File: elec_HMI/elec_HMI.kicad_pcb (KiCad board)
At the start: 2 copper layers, 20 x 20 mm, 17 parts, among them J1 JST SH, J7 JST SH, U1 AS5600L

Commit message: [update] Angle+IMU are routed ERC OK
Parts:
- removed C25: 100n, Capacitor_SMD:C_0402_1005Metric
- removed D1: SP0503BAHT, Package_TO_SOT_SMD:SOT-143
- removed FID1, FID2, FID3: DNP Fiducial, Fiducial:Fiducial_1mm_Mask2mm
- removed G1: qwiic_Logo, Library_Pollen:Logo_qwiic_5mm
- removed H2: Logo HF 2025, Library_Pollen:Logo_HF_2025
- removed H3: DNP Logo Pollen 2021, Library_Pollen:Logo_Pollen_2021_sq
- removed H4: Mounting Holes M2,5, MountingHole:MountingHole_2.7mm_M2.5_ISO7380_Pad_TopBottom
- removed H5: MountingHole_Pad, MountingHole:MountingHole_2.7mm_M2.5_ISO7380_Pad_TopBottom
- removed H6, H7: Centering Hole 2 mm, Library_Pollen:MountingHole_2.0mm
- removed J1, J7: JST SH, Connector_JST:JST_SH_SM04B-SRSS-TB_1x04-1MP_P1.00mm_Horizontal
- removed R1, R2: DNP-10k, Resistor_SMD:R_0402_1005Metric
- removed U1: AS5600L, Package_SO:SOIC-8_3.9x4.9mm_P1.27mm
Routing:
- net +3V3: track 35.5 -> 0.00 mm, vias 2 -> 0
- net Net-(J1-Pin_3): track 22.2 -> 0.00 mm, vias 1 -> 0
- net Net-(J1-Pin_4): track 20.3 -> 0.00 mm, vias 1 -> 0
- net GND: track 9.87 -> 0.00 mm, vias 23 -> 0
- removed copper zone on B.Cu, net GND
- removed copper zone on F.Cu, net GND
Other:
- board outline removed
- board text removed: "!! Prévoir une place pour marquer l'adresse I2C du capteur d'angle"
- board text removed: "ASE001189-A1 angle_sensor"

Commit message: [added] Wiring Diagrams
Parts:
- added C1: 100n 6V3, Capacitor_SMD:C_0402_1005Metric, F.Cu at (127.4, 72.7)
- added D1: SP0503BAHT, Package_TO_SOT_SMD:SOT-143, F.Cu at (142.0, 63.8)
- added D2: Green, LED_SMD:LED_0603_1608Metric, F.Cu at (133.2, 50.4)
- added D3: Red, LED_SMD:LED_0603_1608Metric, F.Cu at (133.2, 53.0)
- added D4: Blue, LED_SMD:LED_0603_1608Metric, F.Cu at (133.2, 55.6)
- added FID1: DNP Fiducial, Fiducial:Fiducial_1mm_Mask2mm, F.Cu at (162.4, 73.3)
- added FID2: DNP Fiducial, Fiducial:Fiducial_1mm_Mask2mm, F.Cu at (133.7, 46.2)
- added FID3: DNP Fiducial, Fiducial:Fiducial_1mm_Mask2mm, F.Cu at (156.4, 46.0)
- added G1: qwiic_Logo, Library_Pollen:Logo_qwiic_5mm, F.Cu at (127.8, 58.7)
- added H2: Logo HF 2025, Library_Pollen:Logo_HF_2025, F.Cu at (161.4, 77.8)
- added H3: DNP Logo Pollen 2021, Library_Pollen:Logo_Pollen_2021_sq, F.Cu at (155.3, 54.6)
- added H4: Mounting Holes M2,5, MountingHole:MountingHole_2.7mm_M2.5_ISO7380_Pad_TopBottom, F.Cu at (127.4, 80.9)
- added H5: MountingHole_Pad, MountingHole:MountingHole_2.7mm_M2.5_ISO7380_Pad_TopBottom, F.Cu at (161.4, 46.5)
- added H6: Centering Hole 2 mm, Library_Pollen:MountingHole_2.0mm, F.Cu at (127.4, 46.6)
- added H7: Centering Hole 2 mm, Library_Pollen:MountingHole_2.0mm, F.Cu at (161.4, 80.6)
- added J1: JST SH, Connector_JST:JST_SH_SM04B-SRSS-TB_1x04-1MP_P1.00mm_Horizontal, F.Cu at (160.8, 63.7)
- added J2: JST SH, Connector_JST:JST_SH_SM04B-SRSS-TB_1x04-1MP_P1.00mm_Horizontal, F.Cu at (128.4, 64.1)
- added R1: 0R, Resistor_SMD:R_0402_1005Metric, F.Cu at (127.5, 74.4)
- added R10: 470R, Resistor_SMD:R_0402_1005Metric, F.Cu at (133.2, 61.2)
- added R2: 0R, Resistor_SMD:R_0402_1005Metric, F.Cu at (127.5, 76.3)
- added R3: DNP-10k, Resistor_SMD:R_0402_1005Metric, F.Cu at (134.2, 64.3)
- added R4: DNP-10k, Resistor_SMD:R_0402_1005Metric, F.Cu at (134.2, 66.3)
- added R5: 0R, Resistor_SMD:R_0402_1005Metric, F.Cu at (127.5, 77.6)
- added R6: 10k, Resistor_SMD:R_0402_1005Metric, F.Cu at (147.6, 63.2)
- added R7: 10k, Resistor_SMD:R_0402_1005Metric, F.Cu at (147.6, 65.1)
- added R8: 470R, Resistor_SMD:R_0402_1005Metric, F.Cu at (133.2, 57.3)
- added R9: 470R, Resistor_SMD:R_0402_1005Metric, F.Cu at (133.2, 59.2)
- added SW1: SW_SPST, Button_Switch_Keyboard:SW_Cherry_MX_1.00u_PCB, F.Cu at (147.6, 49.1)
- added SW2: SW_SPST, Button_Switch_Keyboard:SW_Cherry_MX_1.00u_PCB, F.Cu at (147.5, 68.7)
- added TP1: TestPoint, TestPoint:TestPoint_Loop_D2.50mm_Drill1.0mm_LowProfile, F.Cu at (161.7, 70.1)
- added TP2: TestPoint, TestPoint:TestPoint_Loop_D2.50mm_Drill1.0mm_LowProfile, F.Cu at (158.3, 72.3)
- added U1: PCF8574ATS, Package_SO:SSOP-20_4.4x6.5mm_P0.65mm, F.Cu at (132.7, 73.1)
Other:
- board outline added: 40 x 40 mm

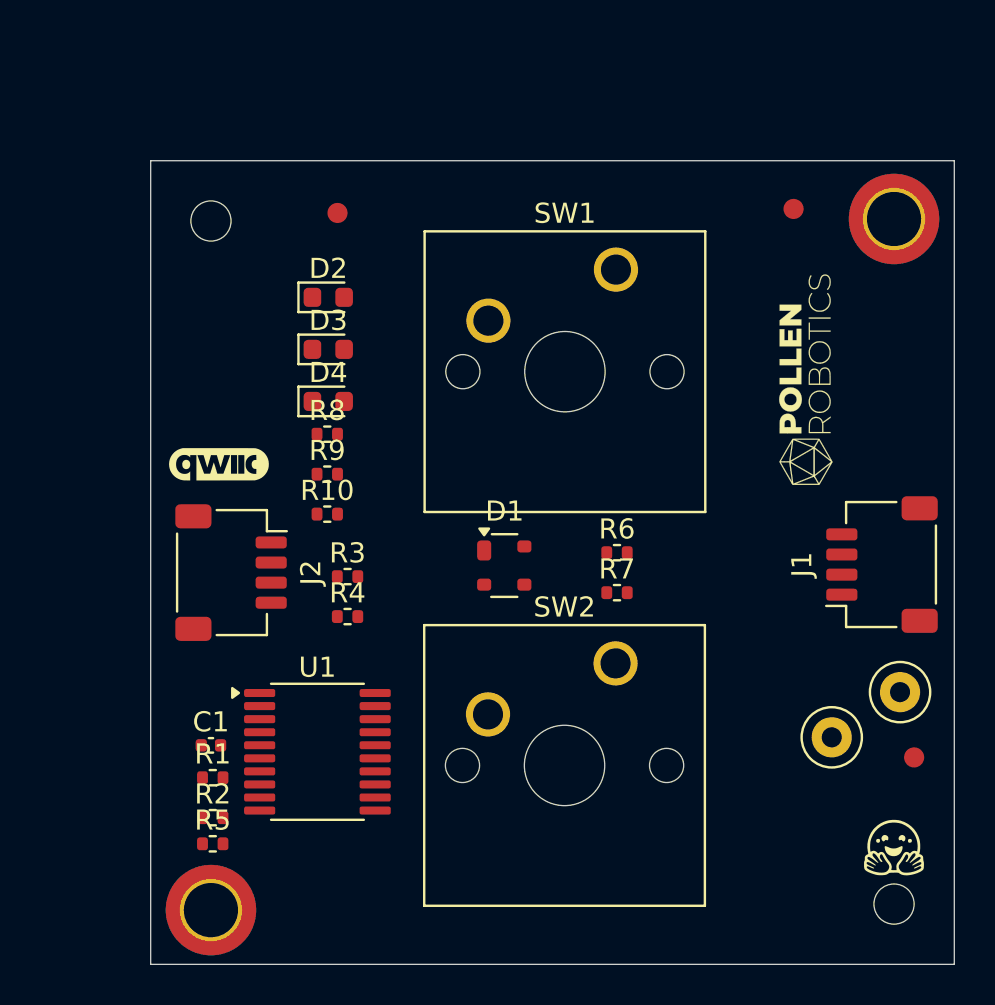
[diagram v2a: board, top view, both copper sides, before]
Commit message: [update] Mechanical adaptations.
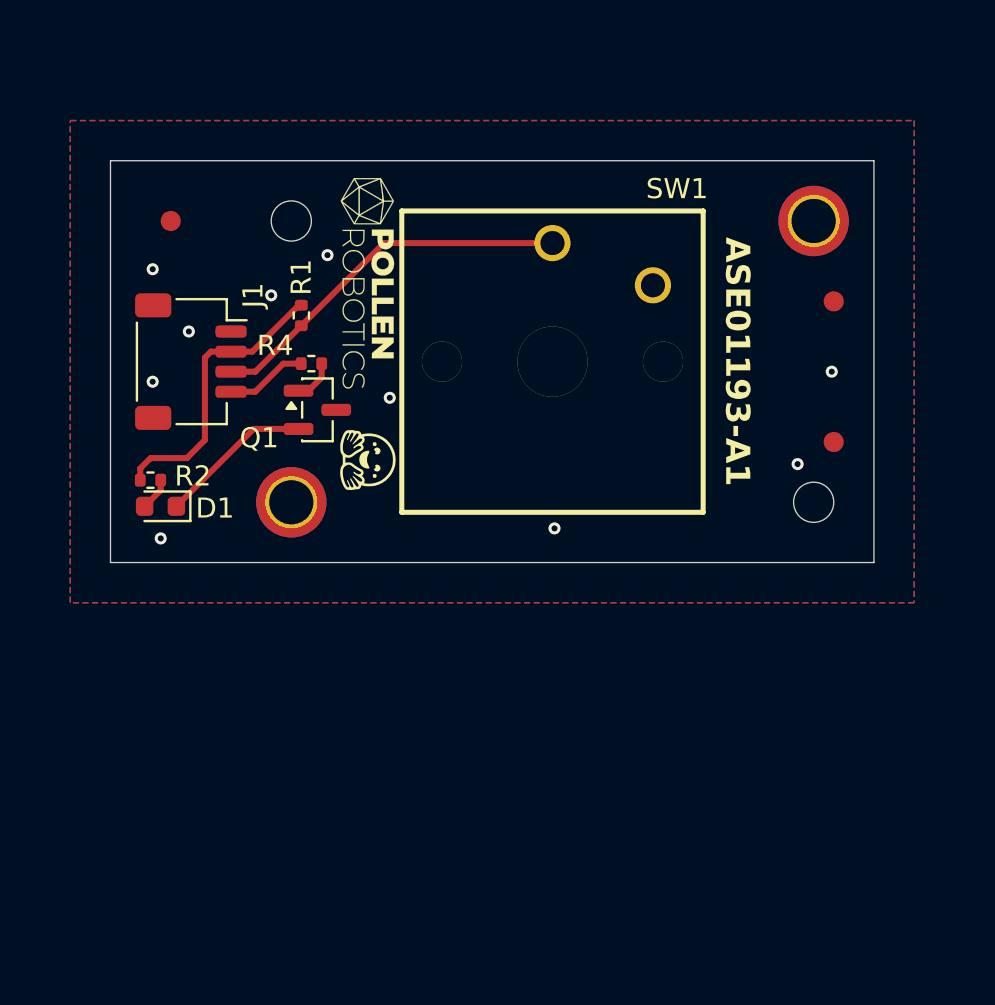
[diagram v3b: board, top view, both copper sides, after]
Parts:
- removed C1: 100n 6V3, Capacitor_SMD:C_0402_1005Metric
- removed the D1 at (142.0, 63.8)
- removed D2: Green, LED_SMD:LED_0603_1608Metric
- removed D4: Blue, LED_SMD:LED_0603_1608Metric
- removed G1: qwiic_Logo, Library_Pollen:Logo_qwiic_5mm
- removed J2: JST SH, Connector_JST:JST_SH_SM04B-SRSS-TB_1x04-1MP_P1.00mm_Horizontal
- removed the R1 at (127.5, 74.4)
- removed R10, R8: 470R, Resistor_SMD:R_0402_1005Metric
- removed the R2 at (127.5, 76.3)
- removed R3: DNP-10k, Resistor_SMD:R_0402_1005Metric
- removed R5: 0R, Resistor_SMD:R_0402_1005Metric
- removed R7: 10k, Resistor_SMD:R_0402_1005Metric
- removed SW2: SW_SPST, Button_Switch_Keyboard:SW_Cherry_MX_1.00u_PCB
- removed TP1, TP2: TestPoint, TestPoint:TestPoint_Loop_D2.50mm_Drill1.0mm_LowProfile
- removed U1: PCF8574ATS, Package_SO:SSOP-20_4.4x6.5mm_P0.65mm
- added Q1: MMBT3906, Package_TO_SOT_SMD:SOT-23, F.Cu at (132.7, 56.0)
- H4: value Mounting Holes M2,5 -> Mounting Holes M2; footprint MountingHole:MountingHole_2.7mm_M2.5_ISO7380_Pad_TopBottom -> MountingHole:MountingHole_2.2mm_M2_ISO7380_Pad_TopBottom
- H5: value MountingHole_Pad -> Mounting Holes M2; footprint MountingHole:MountingHole_2.7mm_M2.5_ISO7380_Pad_TopBottom -> MountingHole:MountingHole_2.2mm_M2_ISO7380_Pad_TopBottom
- R4: value DNP-10k -> 470R
- SW1: footprint Button_Switch_Keyboard:SW_Cherry_MX_1.00u_PCB -> LCSC_parts_lib:KEY-TH_CPG135001D0X
- moved J1 35.9 mm to (126.4, 53.6), turned to -90 degrees
- moved H2 32.5 mm to (135.2, 58.5), turned to -90 degrees
- moved FID1 23.0 mm to (158.4, 50.6)
- moved H4 20.7 mm to (131.4, 60.6)
- moved H7 20.4 mm to (157.4, 60.6)
- moved R1 19.7 mm to (131.9, 51.3), turned to -90 degrees
- moved H3 19.1 mm to (136.9, 49.6), turned to -90 degrees
- moved R4 12.7 mm to (132.4, 53.7), turned to 180 degrees
- moved FID3 11.8 mm to (158.4, 57.6)
- moved D1 11.4 mm to (124.9, 60.8), turned to 180 degrees
- moved R2 8.81 mm to (124.4, 59.5), turned to 180 degrees
- moved FID2 8.31 mm to (125.4, 46.6)
- moved H5 4.00 mm to (157.4, 46.6)
- moved H6 4.00 mm to (131.4, 46.6)
- moved SW1 0.71 mm to (146.9, 48.8)
- renumbered D3 to D1, R6 to R1, R9 to R2
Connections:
- D1 pad 1: GND -> Net-(D1-K)
- R1 pad 2: Net-(SW1-A) -> Net-(J1-Pin_3)
- R2 pad 2: Net-(U1-P4) -> +3V3
- R4 pad 1: +3V3 -> Net-(Q1-B)
- R4 pad 2: Net-(J1-Pin_3) -> Net-(J1-Pin_4)
- SW1 pad 1: Net-(SW1-A) -> Net-(J1-Pin_3)
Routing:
- net Net-(J1-Pin_3): track 0.00 -> 18.7 mm
- net +3V3: track 0.00 -> 14.4 mm
- net Net-(D1-K): track 0.00 -> 7.68 mm
- net Net-(J1-Pin_4): track 0.00 -> 4.07 mm
- net Net-(Q1-B): track 0.00 -> 2.11 mm
- net Net-(D1-A): track 0.00 -> 1.63 mm
- net GND: vias 0 -> 10
- added copper zone on B.Cu, net GND
- added copper zone on F.Cu, net GND
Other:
- board size 40 x 40 mm -> 38 x 20 mm
- board text added: "ASE01193-A1"
